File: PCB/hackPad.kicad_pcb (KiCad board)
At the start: 2 copper layers, 42.9 x 64.3 mm, 7 parts, among them SW1 SW_Push, SW2 SW_Push, SW3 SW_Push, SW4 SW_Push, U1 XIAO-RP2040-DIP

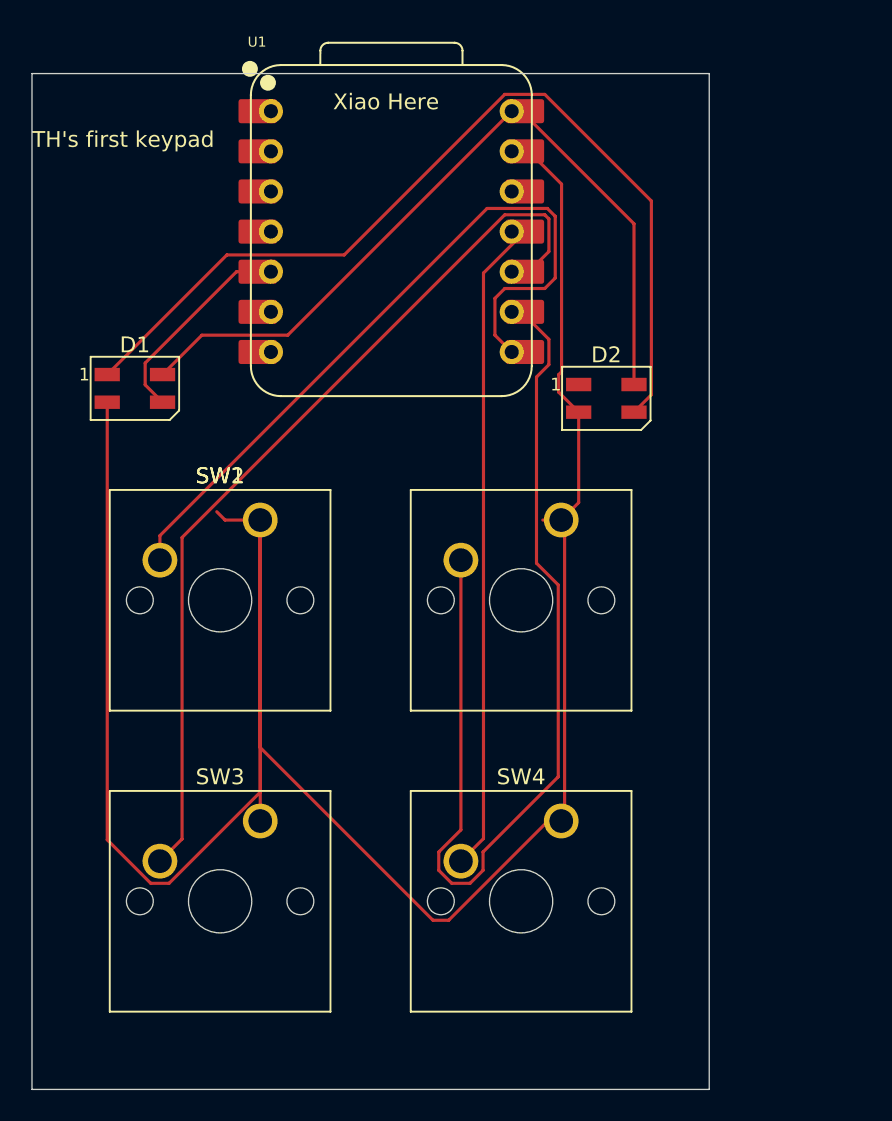
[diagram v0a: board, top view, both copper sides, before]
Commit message: Remade to add more changes to make the pad more unique
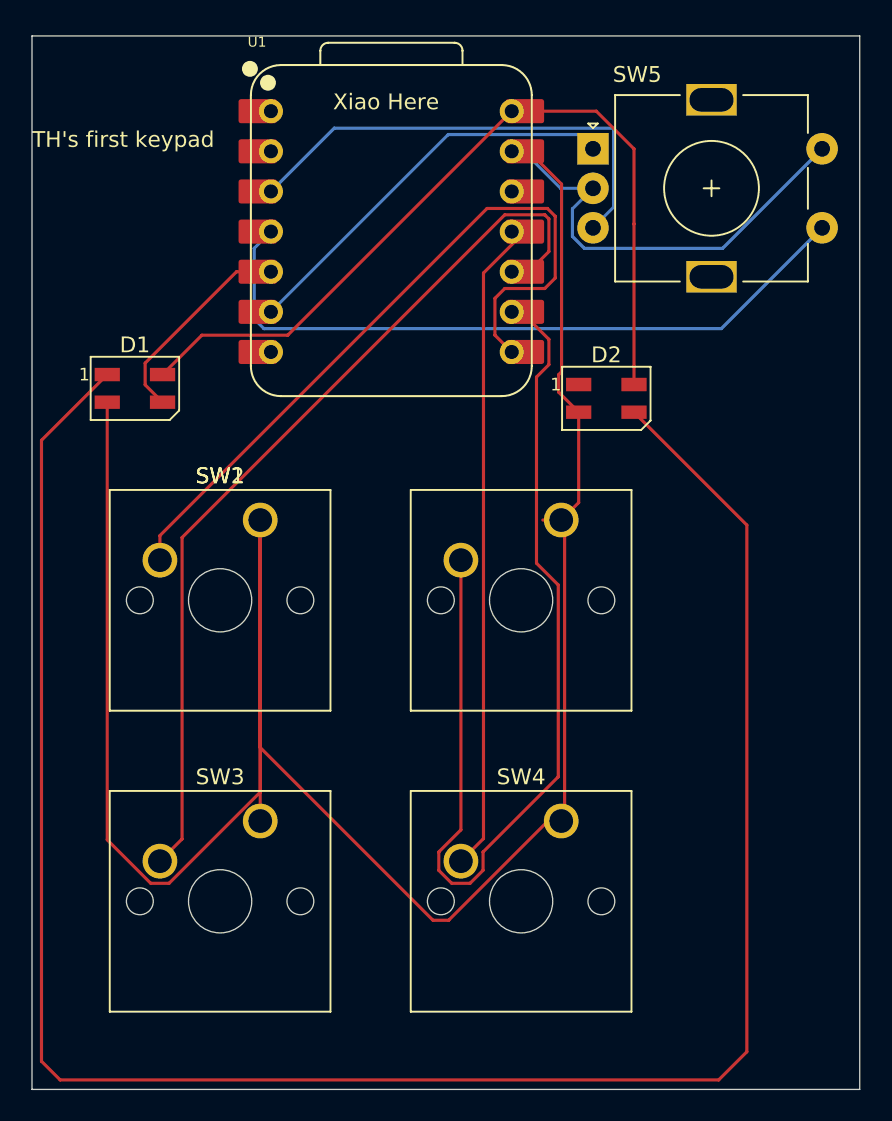
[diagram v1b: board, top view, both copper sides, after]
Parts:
- added SW5: RotaryEncoder_Switch, Rotary_Encoder:RotaryEncoder_Alps_EC11E-Switch_Vertical_H20mm, F.Cu at (156.9, 57.1)
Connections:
- U1 pad 3: unconnected-(U1-GPIO28/ADC2/A2-Pad3) -> Net-(U1-GPIO28/ADC2/A2)
- U1 pad 4: unconnected-(U1-GPIO29/ADC3/A3-Pad4) -> Net-(U1-GPIO29/ADC3/A3)
- U1 pad 6: unconnected-(U1-GPIO7/SCL-Pad6) -> Net-(U1-GPIO7/SCL)
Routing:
- net Net-(D1-DOUT): track 58.4 -> 134.5 mm
- net Net-(U1-GPIO29/ADC3/A3): track 0.00 -> 44.8 mm
- net Net-(U1-GPIO28/ADC2/A2): track 0.00 -> 30.2 mm
- net GND: track 167.0 -> 192.4 mm
- net Net-(U1-GPIO7/SCL): track 0.00 -> 25.4 mm
- net +5V: track 49.9 -> 52.7 mm
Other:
- board size 42.9 x 64.3 mm -> 52.4 x 66.7 mm
